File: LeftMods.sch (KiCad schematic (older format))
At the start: 12 parts

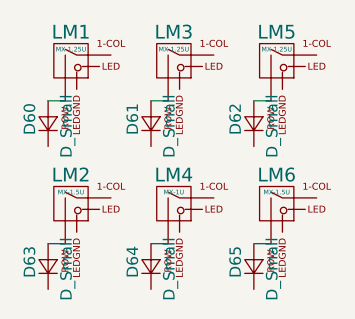
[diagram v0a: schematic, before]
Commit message: Place diodes, remove duplicates
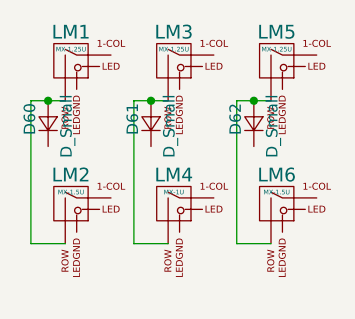
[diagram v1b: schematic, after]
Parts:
- removed D63, D64, D65: D_Small, Diodes_SMD:D_SOD-123, symbol D_Small
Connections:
- net at D60.2 (A), LM1.2 (ROW): now also LM2.2 (ROW)
- net at D61.2 (A), LM3.2 (ROW): now also LM4.2 (ROW)
- net at D62.2 (A), LM5.2 (ROW): now also LM6.2 (ROW)
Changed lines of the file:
@@
 $EndComp
 Wire Wire Line
-	2300 2400 2225 2400
+	2150 2400 2300 2400
 $Comp
 L MX-1U LM3
@@
 $EndComp
 Wire Wire Line
-	2750 2400 2675 2400
+	2600 2400 2750 2400
 $Comp
 L MX-1U LM5
@@
 $EndComp
 Wire Wire Line
-	3200 2400 3125 2400
+	3050 2400 3200 2400
 $Comp
 L MX-1U LM2
@@
 	1    0    0    -1
 $EndComp
-$Comp
-L D_Small D63
-U 1 1 5A68E98F
-P 2225 3125
-F 0 "D63" H 2175 3205 50  0000 L CNN
-F 1 "D_Small" H 2075 3045 50  0000 L CNN
-F 2 "Diodes_SMD:D_SOD-123" V 2225 3125 50  0001 C CNN
-F 3 "" V 2225 3125 50  0001 C CNN
-	1    2225 3125
-	0    -1   -1   0
-$EndComp
 Wire Wire Line
-	2300 3025 2225 3025
+	2150 3025 2300 3025
 $Comp
 L MX-1U LM4
@@
 	1    0    0    -1
 $EndComp
-$Comp
-L D_Small D64
-U 1 1 5A68E99E
-P 2675 3125
-F 0 "D64" H 2625 3205 50  0000 L CNN
-F 1 "D_Small" H 2525 3045 50  0000 L CNN
-F 2 "Diodes_SMD:D_SOD-123" V 2675 3125 50  0001 C CNN
-F 3 "" V 2675 3125 50  0001 C CNN
-	1    2675 3125
-	0    -1   -1   0
-$EndComp
 Wire Wire Line
-	2750 3025 2675 3025
+	2600 3025 2750 3025
 $Comp
 L MX-1U LM6
@@
 	1    0    0    -1
 $EndComp
-$Comp
-L D_Small D65
-U 1 1 5A68E9AD
-P 3125 3125
-F 0 "D65" H 3075 3205 50  0000 L CNN
-F 1 "D_Small" H 2975 3045 50  0000 L CNN
-F 2 "Diodes_SMD:D_SOD-123" V 3125 3125 50  0001 C CNN
-F 3 "" V 3125 3125 50  0001 C CNN
-	1    3125 3125
-	0    -1   -1   0
-$EndComp
 Wire Wire Line
-	3200 3025 3125 3025
+	3050 3025 3200 3025
+Wire Wire Line
+	3050 2400 3050 3025
+Connection ~ 3125 2400
+Wire Wire Line
+	2600 2400 2600 3025
+Connection ~ 2675 2400
+Wire Wire Line
+	2150 2400 2150 3025
+Connection ~ 2225 2400
 $EndSCHEMATC

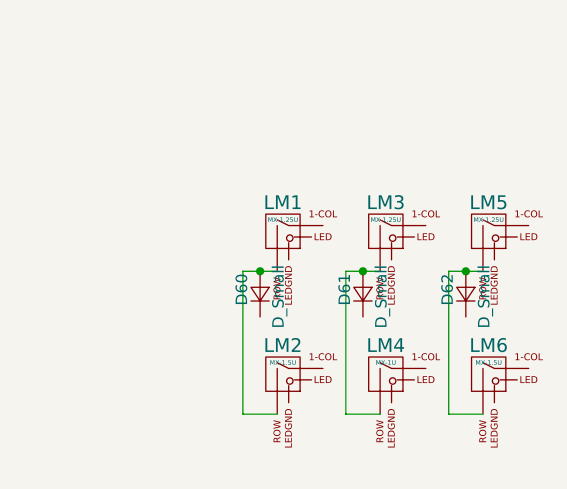
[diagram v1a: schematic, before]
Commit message: Add basic row col to subsheets
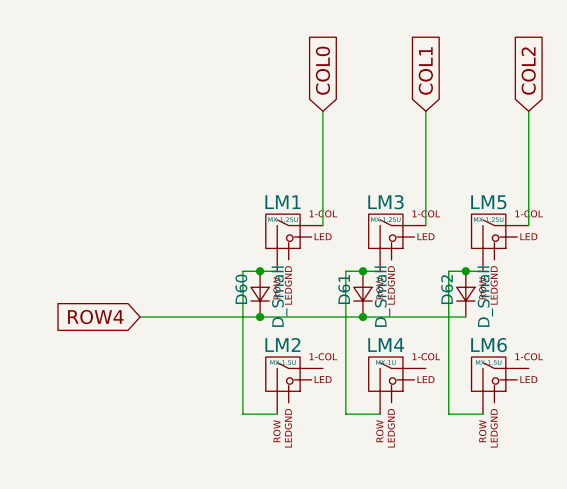
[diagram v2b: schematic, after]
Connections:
- net COL0: now reaches LM1.1 (COL)
- net ROW4: now reaches D60.1 (K)
- net ROW4: now also D61.1 (K), D62.1 (K)
- net COL1: now reaches LM3.1 (COL)
- net COL2: now reaches LM5.1 (COL)
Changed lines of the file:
@@
 	2150 2400 2150 3025
 Connection ~ 2225 2400
+Wire Wire Line
+	2500 2200 2500 1700
+Text GLabel 2500 1700 1    60   Input ~ 0
+COL0
+Wire Wire Line
+	2950 2200 2950 1700
+Text GLabel 2950 1700 1    60   Input ~ 0
+COL1
+Wire Wire Line
+	3400 2200 3400 1700
+Text GLabel 3400 1700 1    60   Input ~ 0
+COL2
+Wire Wire Line
+	1700 2600 3125 2600
+Text GLabel 1700 2600 0    60   Input ~ 0
+ROW4
+Connection ~ 2225 2600
+Connection ~ 2675 2600
 $EndSCHEMATC

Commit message: Pinout right mods
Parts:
- LM2, LM6: footprint MX_Alps_Hybrid:MX-1.5U -> MX_Alps_Hybrid:MX-1.5U-FLIPPED
- LM4: footprint MX_Alps_Hybrid:MX-1U -> MX_Alps_Hybrid:MX-1U-FLIPPED
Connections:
- net COL0: now also LM2.1 (COL)
- net COL1: now also LM4.1 (COL)
- net COL2: now also LM6.1 (COL)
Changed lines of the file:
@@
 F 0 "LM2" H 2325 2975 60  0000 C CNN
 F 1 "MX-1.5U" H 2325 2900 20  0000 C CNN
-F 2 "MX_Alps_Hybrid:MX-1.5U" H 2300 2825 60  0001 C CNN
+F 2 "MX_Alps_Hybrid:MX-1.5U-FLIPPED" H 2300 2825 60  0001 C CNN
 F 3 "" H 2300 2825 60  0001 C CNN
 	1    2325 2850
@@
 F 0 "LM4" H 2775 2975 60  0000 C CNN
 F 1 "MX-1U" H 2775 2900 20  0000 C CNN
-F 2 "MX_Alps_Hybrid:MX-1U" H 2750 2825 60  0001 C CNN
+F 2 "MX_Alps_Hybrid:MX-1U-FLIPPED" H 2750 2825 60  0001 C CNN
 F 3 "" H 2750 2825 60  0001 C CNN
 	1    2775 2850
@@
 F 0 "LM6" H 3225 2975 60  0000 C CNN
 F 1 "MX-1.5U" H 3225 2900 20  0000 C CNN
-F 2 "MX_Alps_Hybrid:MX-1.5U" H 3200 2825 60  0001 C CNN
+F 2 "MX_Alps_Hybrid:MX-1.5U-FLIPPED" H 3200 2825 60  0001 C CNN
 F 3 "" H 3200 2825 60  0001 C CNN
 	1    3225 2850
@@
 Connection ~ 2225 2400
 Wire Wire Line
-	2500 2200 2500 1700
+	2500 1700 2500 2825
 Text GLabel 2500 1700 1    60   Input ~ 0
 COL0
 Wire Wire Line
-	2950 2200 2950 1700
+	2950 1700 2950 2825
 Text GLabel 2950 1700 1    60   Input ~ 0
 COL1
 Wire Wire Line
-	3400 2200 3400 1700
+	3400 1700 3400 2825
 Text GLabel 3400 1700 1    60   Input ~ 0
 COL2
@@
 Connection ~ 2225 2600
 Connection ~ 2675 2600
+Connection ~ 2500 2200
+Connection ~ 2950 2200
+Connection ~ 3400 2200
 $EndSCHEMATC

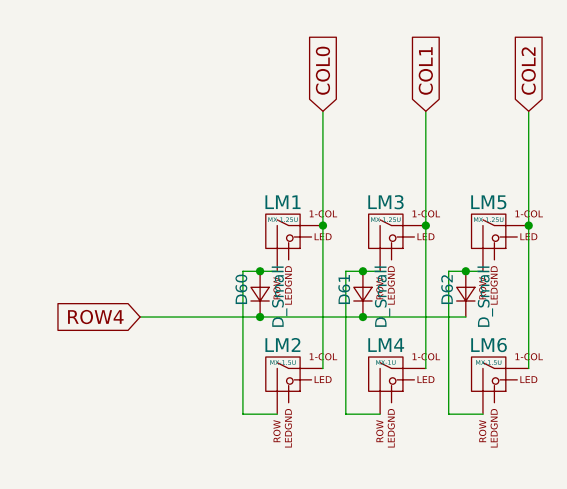
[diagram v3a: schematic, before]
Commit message: Route left half LED rows
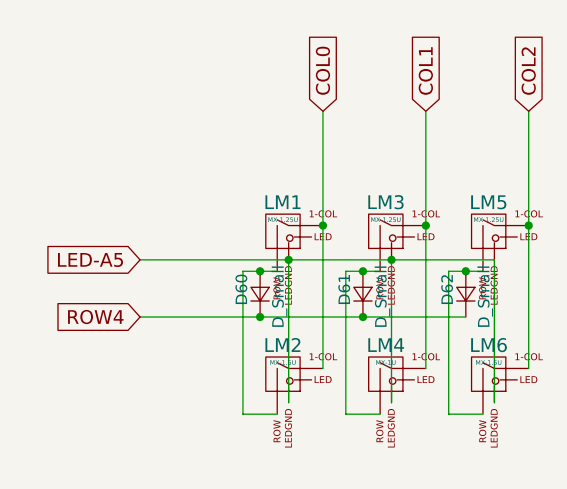
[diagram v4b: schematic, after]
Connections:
- net LED-A5: now reaches LM1.4 (LEDGND)
- net LED-A5: now also LM2.4 (LEDGND), LM3.4 (LEDGND), LM4.4 (LEDGND), LM5.4 (LEDGND), LM6.4 (LEDGND)
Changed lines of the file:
@@
 Connection ~ 2950 2200
 Connection ~ 3400 2200
+Wire Wire Line
+	1700 2350 3250 2350
+Connection ~ 2800 2350
+Connection ~ 2350 2350
+Text GLabel 1700 2350 0    60   Input ~ 0
+LED-A5
+Wire Wire Line
+	2350 2350 2350 2975
+Wire Wire Line
+	2800 2975 2800 2350
+Wire Wire Line
+	3250 2350 3250 2975
 $EndSCHEMATC

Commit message: Unroute LEDs
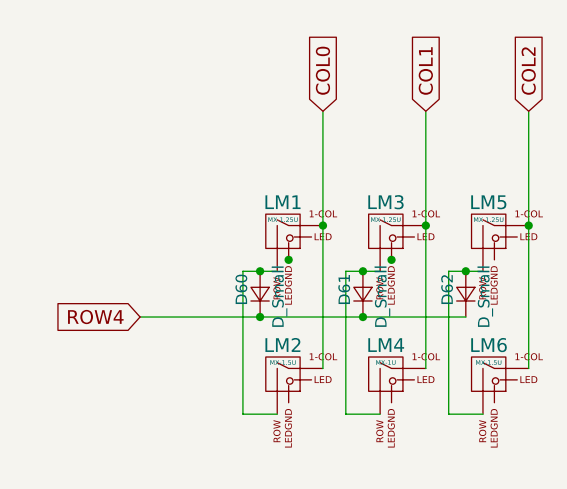
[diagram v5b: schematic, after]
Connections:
- removed net LED-A5: LM1.4 (LEDGND), LM2.4 (LEDGND), LM3.4 (LEDGND), LM4.4 (LEDGND), LM5.4 (LEDGND), LM6.4 (LEDGND)
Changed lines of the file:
@@
 Connection ~ 2950 2200
 Connection ~ 3400 2200
-Wire Wire Line
-	1700 2350 3250 2350
 Connection ~ 2800 2350
 Connection ~ 2350 2350
-Text GLabel 1700 2350 0    60   Input ~ 0
-LED-A5
-Wire Wire Line
-	2350 2350 2350 2975
-Wire Wire Line
-	2800 2975 2800 2350
-Wire Wire Line
-	3250 2350 3250 2975
 $EndSCHEMATC

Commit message: Swap footprints for No-LED counterparts
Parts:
- LM1, LM3, LM5: footprint MX_Alps_Hybrid:MX-1.25U -> MX_Alps_Hybrid:MX-1.25U-NoLED
- LM2, LM6: footprint MX_Alps_Hybrid:MX-1.5U-FLIPPED -> MX_Alps_Hybrid:MX-1.5U-NoLED
- LM4: footprint MX_Alps_Hybrid:MX-1U-FLIPPED -> MX_Alps_Hybrid:MX-1U-NoLED
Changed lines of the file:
@@
 F 0 "LM1" H 2325 2350 60  0000 C CNN
 F 1 "MX-1.25U" H 2325 2275 20  0000 C CNN
-F 2 "MX_Alps_Hybrid:MX-1.25U" H 2300 2200 60  0001 C CNN
+F 2 "MX_Alps_Hybrid:MX-1.25U-NoLED" H 2300 2200 60  0001 C CNN
 F 3 "" H 2300 2200 60  0001 C CNN
 	1    2325 2225
@@
 F 0 "LM3" H 2775 2350 60  0000 C CNN
 F 1 "MX-1.25U" H 2775 2275 20  0000 C CNN
-F 2 "MX_Alps_Hybrid:MX-1.25U" H 2750 2200 60  0001 C CNN
+F 2 "MX_Alps_Hybrid:MX-1.25U-NoLED" H 2750 2200 60  0001 C CNN
 F 3 "" H 2750 2200 60  0001 C CNN
 	1    2775 2225
@@
 F 0 "LM5" H 3225 2350 60  0000 C CNN
 F 1 "MX-1.25U" H 3225 2275 20  0000 C CNN
-F 2 "MX_Alps_Hybrid:MX-1.25U" H 3200 2200 60  0001 C CNN
+F 2 "MX_Alps_Hybrid:MX-1.25U-NoLED" H 3200 2200 60  0001 C CNN
 F 3 "" H 3200 2200 60  0001 C CNN
 	1    3225 2225
@@
 F 0 "LM2" H 2325 2975 60  0000 C CNN
 F 1 "MX-1.5U" H 2325 2900 20  0000 C CNN
-F 2 "MX_Alps_Hybrid:MX-1.5U-FLIPPED" H 2300 2825 60  0001 C CNN
+F 2 "MX_Alps_Hybrid:MX-1.5U-NoLED" H 2300 2825 60  0001 C CNN
 F 3 "" H 2300 2825 60  0001 C CNN
 	1    2325 2850
@@
 F 0 "LM4" H 2775 2975 60  0000 C CNN
 F 1 "MX-1U" H 2775 2900 20  0000 C CNN
-F 2 "MX_Alps_Hybrid:MX-1U-FLIPPED" H 2750 2825 60  0001 C CNN
+F 2 "MX_Alps_Hybrid:MX-1U-NoLED" H 2750 2825 60  0001 C CNN
 F 3 "" H 2750 2825 60  0001 C CNN
 	1    2775 2850
@@
 F 0 "LM6" H 3225 2975 60  0000 C CNN
 F 1 "MX-1.5U" H 3225 2900 20  0000 C CNN
-F 2 "MX_Alps_Hybrid:MX-1.5U-FLIPPED" H 3200 2825 60  0001 C CNN
+F 2 "MX_Alps_Hybrid:MX-1.5U-NoLED" H 3200 2825 60  0001 C CNN
 F 3 "" H 3200 2825 60  0001 C CNN
 	1    3225 2850
